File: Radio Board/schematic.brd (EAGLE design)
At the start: 55 x 60 mm, 3 parts, among them U1 XBP9X-DMRS-001

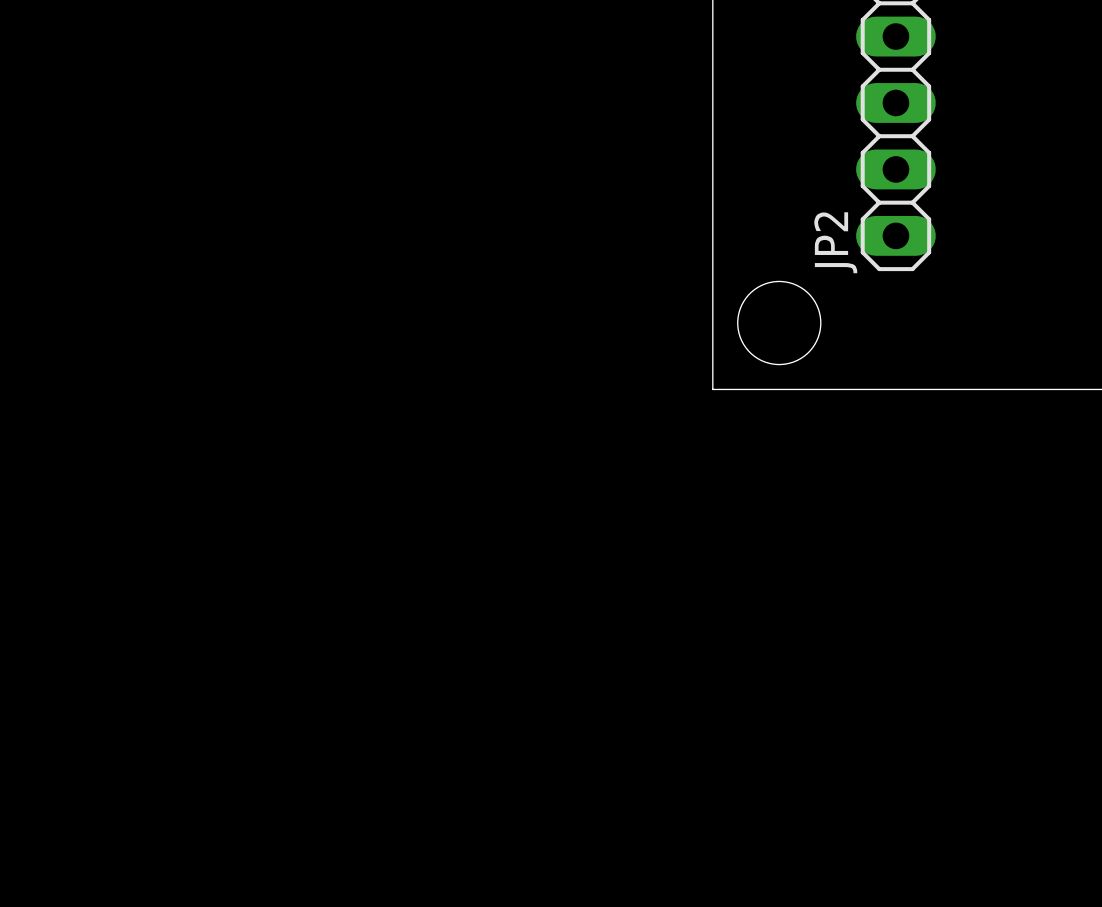
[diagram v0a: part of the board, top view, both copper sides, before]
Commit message: Added GPS module and complementary components
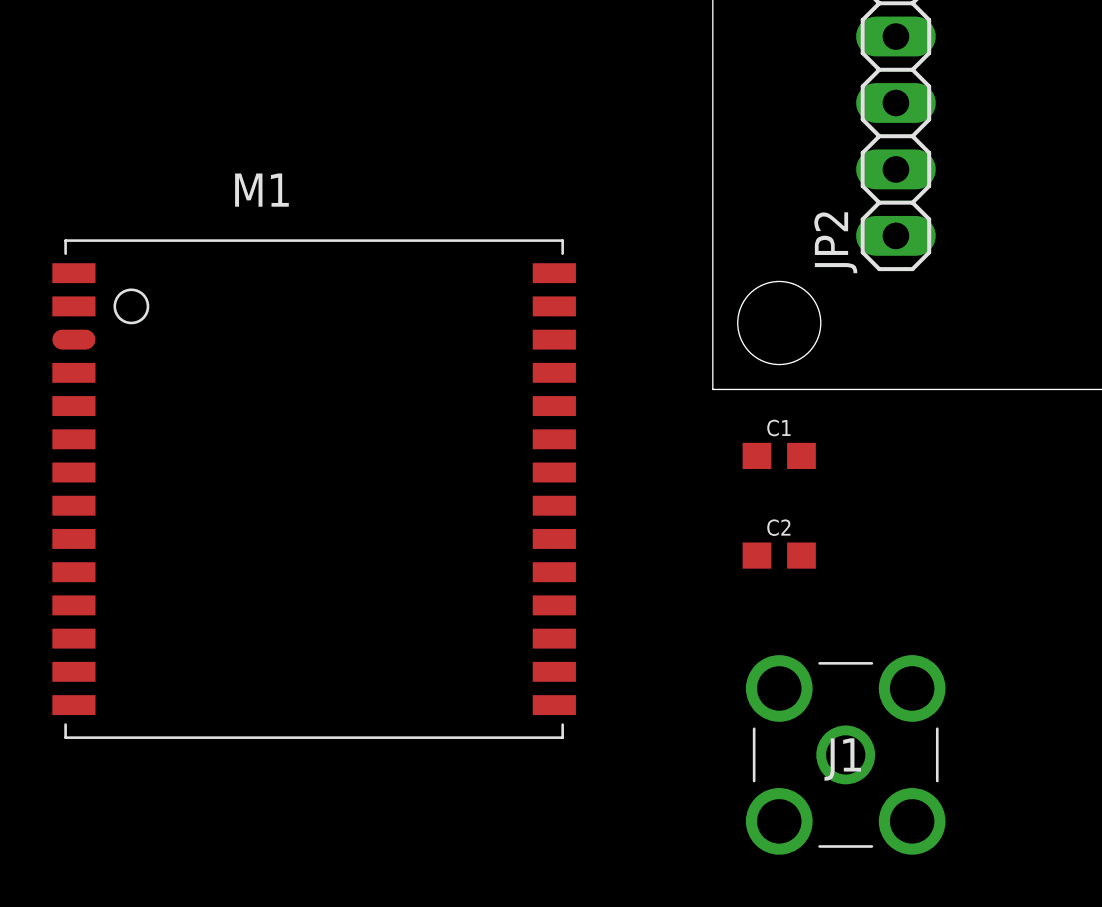
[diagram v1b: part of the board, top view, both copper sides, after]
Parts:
- added C1: 1uF, SparkFun-Capacitors:0603
- added C2: 100pF, SparkFun-Capacitors:0603
- added J1: 132134RP, 132134RP:132134RP
- added M1: (no value), trimble:1919
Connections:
- removed net VCC: U1.2
- new net N$1: J1.1, U1.36
- net 3.3V: now also C1.1, C2.1, M1.12, U1.2
- net GND: now also C1.2, C2.2, J1.2, J1.3, J1.4, J1.5, M1.1, M1.13, M1.14, M1.15, M1.2, M1.27, M1.28, M1.4
- net RX1: now also M1.23
- net RX2: now also U1.3
- net TX1: now also M1.21
- net TX2: now also U1.4

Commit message: Finished wiring
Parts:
- removed M1: (no value), trimble:1919
- removed U1: XBP9X-DMRS-001, XBP9X-DMRS-001:MODULE_XBP9X-DMRS-001
- added GPS, J3: (no value), SparkFun-Connectors:1X10_NO_SILK
- added RADIO: XBP9X-DMRS-001, XBP9X-DMRS-001:MODULE_XBP9X-DMRS-001
- moved J1 47.1 mm to (47.0, 7.62)
- moved C2 44.0 mm to (24.1, 32.0), turned to 90 degrees
- moved C1 36.8 mm to (15.2, 32.0), turned to 90 degrees
- moved JP1 14.0 mm to (48.0, 44.0)
- moved JP2 14.0 mm to (7.00, 44.0)
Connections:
- removed net N$1: J1.1, U1.36
- new net RF: J1.1, RADIO.36
- net 3.3V: now also J3.8, RADIO.2; no longer M1.12, U1.2
- net GND: now also J3.9, RADIO.1, RADIO.11, RADIO.13, RADIO.22, RADIO.35, RADIO.38, RADIO.V38_1, RADIO.V38_2, RADIO.V38_3, RADIO.V38_4, RADIO.V38_5, RADIO.V38_6, RADIO.V38_7, RADIO.V38_8, RADIO.V38_9; no longer M1.1, M1.13, M1.14, M1.15, M1.2, M1.27, M1.28, M1.4, U1.1, U1.11, U1.13, U1.22, U1.35, U1.38, U1.V38_1, U1.V38_2, U1.V38_3, U1.V38_4, U1.V38_5, U1.V38_6, U1.V38_7, U1.V38_8, U1.V38_9
- net RX1: now also GPS.7; no longer M1.23
- net RX2: now also RADIO.3; no longer U1.3
- net TX1: now also GPS.5; no longer M1.21
- net TX2: now also RADIO.4; no longer U1.4
- net VREF: now also RADIO.27; no longer U1.27
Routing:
- net 3.3V: track 0.00 -> 74.9 mm
- net RF: track 0.00 -> 69.8 mm
- net TX1: track 0.00 -> 50.9 mm
- net RX1: track 0.00 -> 41.4 mm
- net RX2: track 0.00 -> 13.7 mm
- net TX2: track 0.00 -> 13.5 mm
- added copper zone on layer 1, net GND
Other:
- board size 55 x 60 mm -> 55 x 74 mm

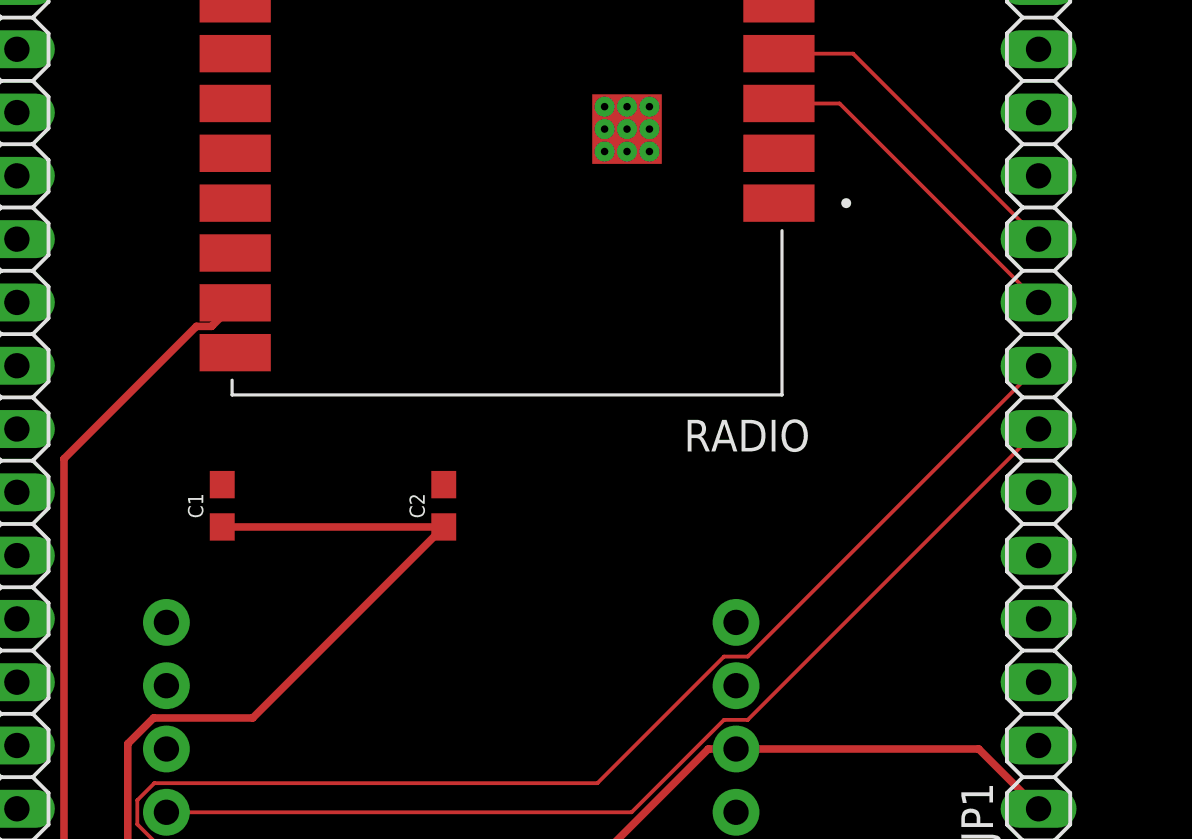
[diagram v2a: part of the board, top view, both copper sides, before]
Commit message: Finished Routing
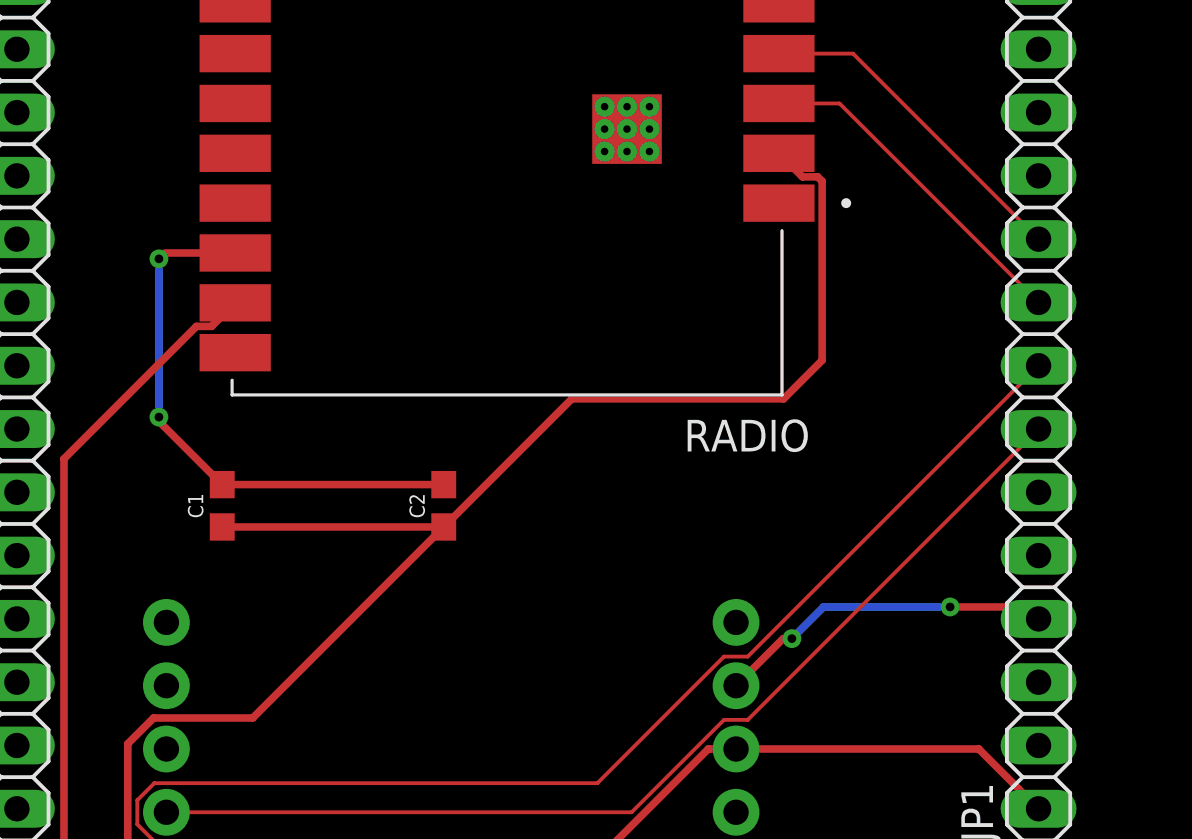
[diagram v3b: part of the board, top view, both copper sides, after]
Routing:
- net GND: track 0.00 -> 35.8 mm, vias 0 -> 4
- net 3.3V: track 74.9 -> 102.2 mm
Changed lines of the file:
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@@
 <drawing>
 <settings>
-<setting alwaysvectorfont="no"/>
+<setting alwaysvectorfont="yes"/>
 <setting verticaltext="up"/>
 </settings>
@@
 <vertex x="0" y="0"/>
 </polygon>
+<wire x1="15.24" y1="32.85" x2="24.13" y2="32.85" width="0.3048" layer="1"/>
+<wire x1="15.24" y1="32.85" x2="12.7" y2="35.39" width="0.3048" layer="1"/>
+<wire x1="12.7" y1="35.39" x2="12.7" y2="35.56" width="0.1524" layer="1"/>
+<via x="12.7" y="35.56" extent="1-16" drill="0.35"/>
+<wire x1="12.7" y1="35.56" x2="12.7" y2="41.91" width="0.3048" layer="16"/>
+<via x="12.7" y="41.91" extent="1-16" drill="0.35"/>
+<wire x1="12.7" y1="41.91" x2="12.935" y2="42.145" width="0.1524" layer="1"/>
+<wire x1="12.935" y1="42.145" x2="15.76" y2="42.145" width="0.3048" layer="1"/>
+<wire x1="35.86" y1="24.78" x2="37.75" y2="26.67" width="0.3048" layer="1"/>
+<wire x1="37.75" y1="26.67" x2="38.1" y2="26.67" width="0.3048" layer="1"/>
+<via x="38.1" y="26.67" extent="1-16" drill="0.35"/>
+<wire x1="38.1" y1="26.67" x2="39.37" y2="27.94" width="0.3048" layer="16"/>
+<wire x1="39.37" y1="27.94" x2="44.45" y2="27.94" width="0.3048" layer="16"/>
+<via x="44.45" y="27.94" extent="1-16" drill="0.35"/>
+<wire x1="44.45" y1="27.94" x2="47.52" y2="27.94" width="0.3048" layer="1"/>
+<wire x1="47.52" y1="27.94" x2="48" y2="27.46" width="0.3048" layer="1"/>
+<wire x1="32.384" y1="46.217" x2="37.58" y2="44.145" width="0" layer="19" extent="1-1"/>
 <wire x1="32.384" y1="47.117" x2="32.384" y2="46.217" width="0" layer="19" extent="1-1"/>
 <wire x1="30.584" y1="46.217" x2="30.584" y2="47.117" width="0" layer="19" extent="1-1"/>
 <wire x1="32.384" y1="48.017" x2="31.484" y2="48.017" width="0" layer="19" extent="1-1"/>
-<wire x1="30.584" y1="48.017" x2="30.584" y2="47.117" width="0" layer="19" extent="1-1"/>
-<wire x1="37.58" y1="44.145" x2="32.384" y2="46.217" width="0" layer="19" extent="1-1"/>
-<wire x1="35.86" y1="24.78" x2="48" y2="27.46" width="0" layer="19" extent="1-1"/>
+<wire x1="30.584" y1="48.017" x2="31.484" y2="48.017" width="0" layer="19" extent="1-1"/>
+<wire x1="24.13" y1="32.85" x2="30.584" y2="46.217" width="0" layer="19" extent="1-1"/>
 </signal>
 <signal name="3.3V">
@@
 <wire x1="11.4506" y1="14.40926875" x2="11.4506" y2="22.45073125" width="0.3048" layer="1"/>
 <wire x1="24.13" y1="31.15" x2="15.24" y2="31.15" width="0.3048" layer="1"/>
-<wire x1="24.13" y1="31.15" x2="37.58" y2="46.145" width="0" layer="19" extent="1-1"/>
+<wire x1="39.13625" y1="45.1998" x2="39.3148" y2="45.02125" width="0.3048" layer="1"/>
+<wire x1="37.58" y1="46.145" x2="38.5252" y2="45.1998" width="0.3048" layer="1"/>
+<wire x1="38.5252" y1="45.1998" x2="39.13625" y2="45.1998" width="0.3048" layer="1"/>
+<wire x1="39.3148" y1="45.02125" x2="39.3148" y2="37.8372" width="0.3048" layer="1"/>
+<wire x1="39.3148" y1="37.8372" x2="37.7692" y2="36.2916" width="0.3048" layer="1"/>
+<wire x1="37.7692" y1="36.2916" x2="29.2716" y2="36.2916" width="0.3048" layer="1"/>
+<wire x1="29.2716" y1="36.2916" x2="24.13" y2="31.15" width="0.3048" layer="1"/>
 </signal>
 <signal name="5V">

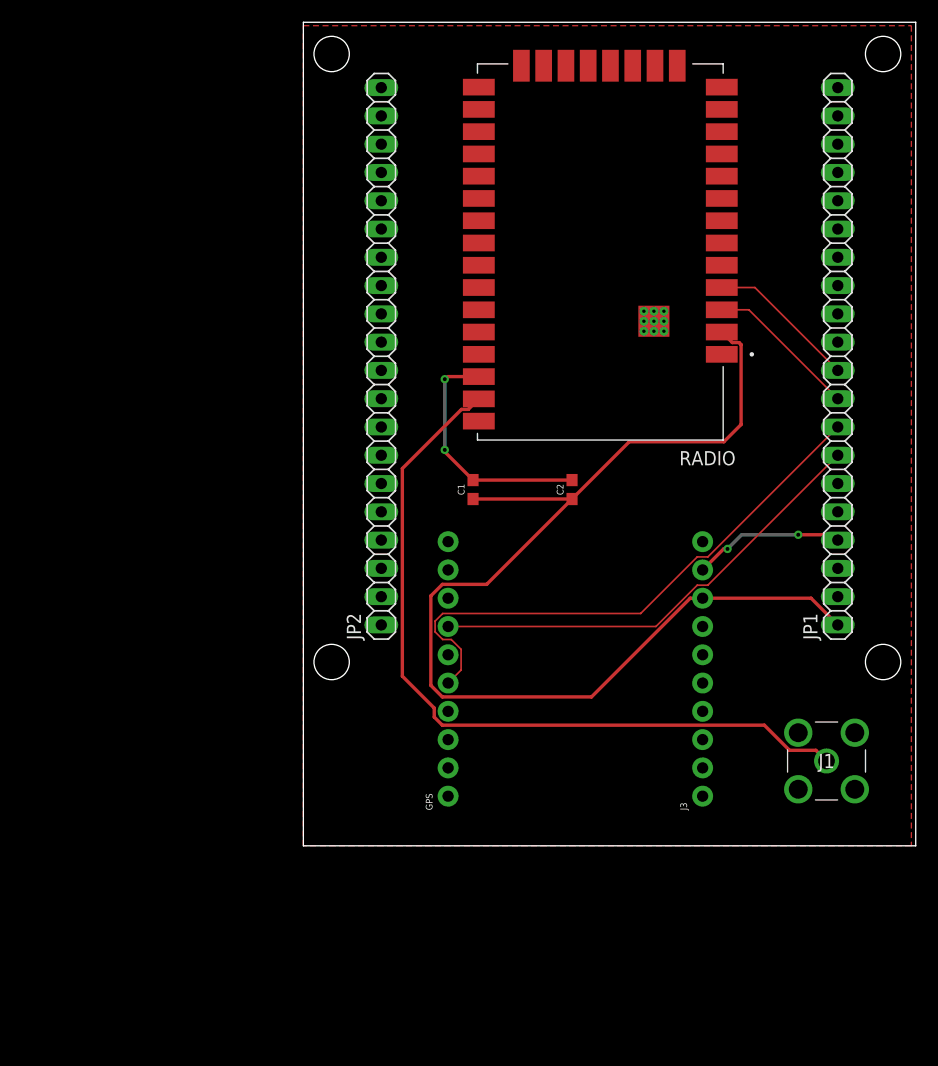
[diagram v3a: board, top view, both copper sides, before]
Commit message: Updated radio & GPS
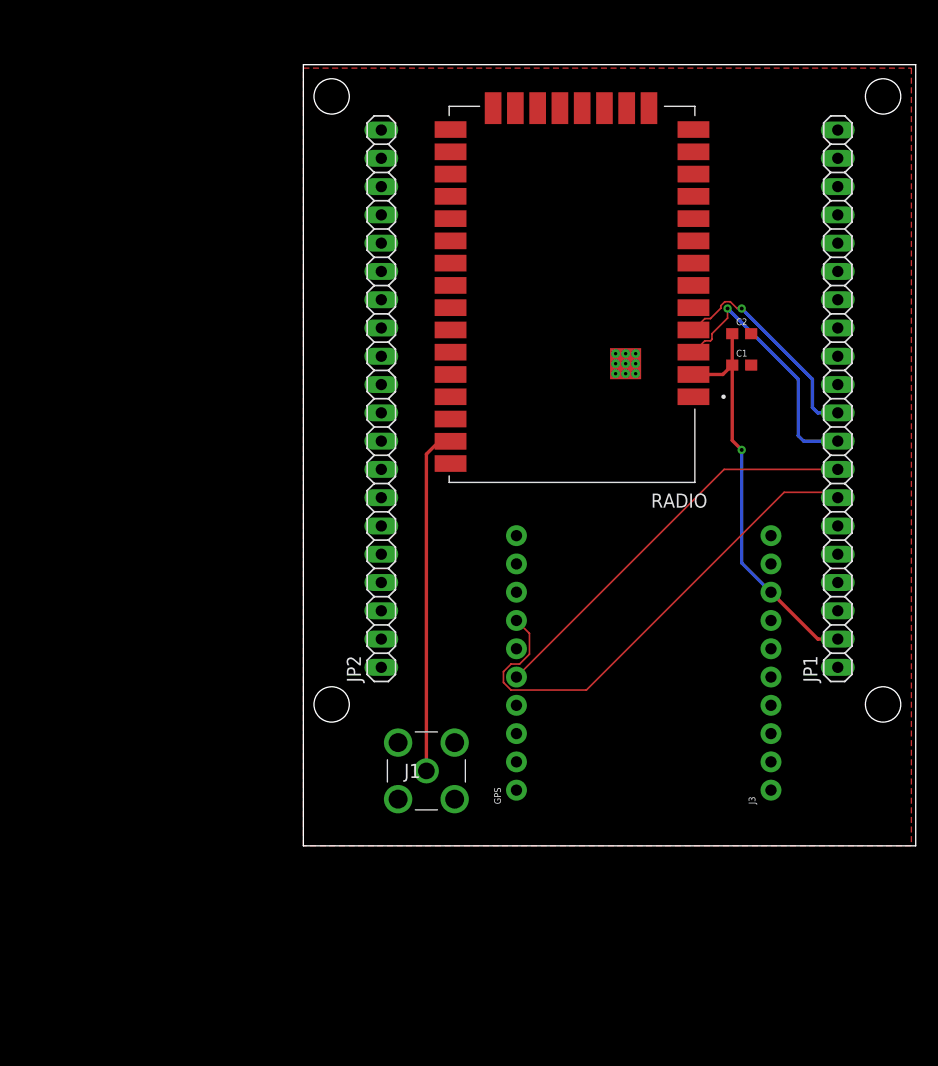
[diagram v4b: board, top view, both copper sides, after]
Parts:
- moved J1 36.0 mm to (11.0, 6.73)
- moved C1 26.6 mm to (39.4, 43.2), turned to 0 degrees
- moved C2 20.7 mm to (39.4, 46.0), turned to 0 degrees
- moved GPS 6.16 mm to (19.1, 5.00)
- moved J3 6.16 mm to (42.0, 5.00)
- moved RADIO 4.58 mm to (24.1, 49.5)
- moved JP1 3.81 mm to (48.0, 40.2)
- moved JP2 3.81 mm to (7.00, 40.2)
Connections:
- removed net 3.3V: C1.1, C2.1, J3.8, JP1.1, RADIO.2
- removed net 5V: JP1.2
- new net 3V3.1: JP1.1
- new net 3V3.2: C1.1, C2.1, J3.8, JP1.2, RADIO.2
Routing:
- net 3.3V: track 102.2 -> 0.00 mm
- net RF: track 69.8 -> 30.8 mm
- net 3V3.2: track 0.00 -> 36.2 mm, vias 0 -> 1
- net GND: track 35.8 -> 0.00 mm, vias 4 -> 0
- net TX1: track 50.9 -> 36.6 mm
- net RX2: track 13.7 -> 24.0 mm, vias 0 -> 1
- net TX2: track 13.5 -> 20.4 mm, vias 0 -> 1
- net RX1: track 41.4 -> 45.3 mm
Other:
- board size 55 x 74 mm -> 55 x 70.2 mm
